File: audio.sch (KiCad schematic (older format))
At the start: 37 parts

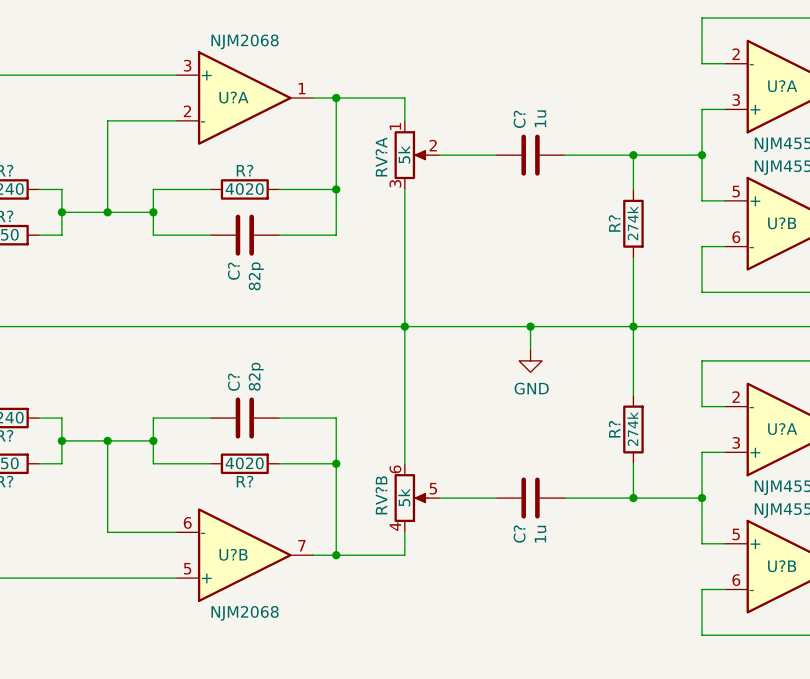
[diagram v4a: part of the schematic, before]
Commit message: replace bourns audio pot for alps (target jade version)
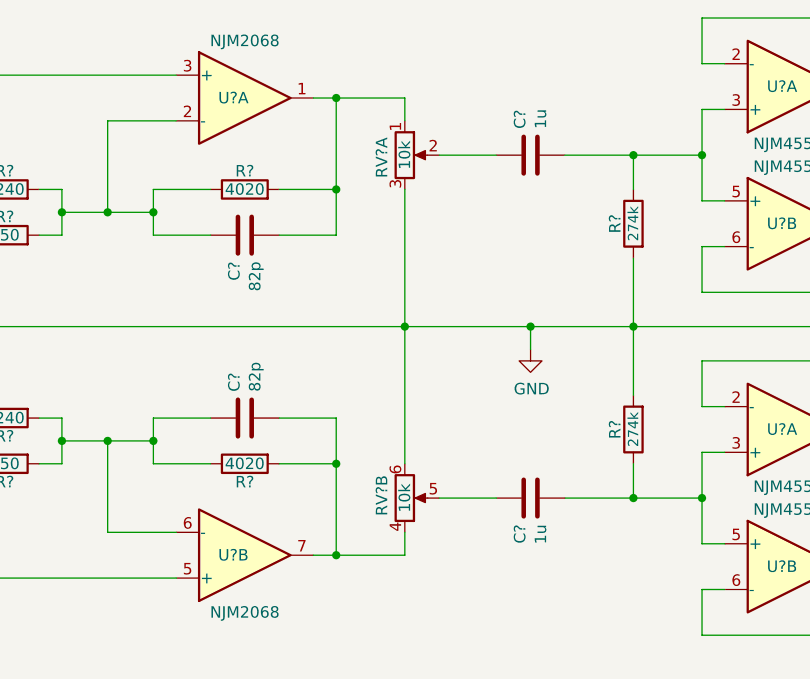
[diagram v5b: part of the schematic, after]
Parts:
- RV?: value 5k -> 10k; footprint bourns:PTD902-1015K-A502 -> Potentiometer_THT:Potentiometer_Alps_RK097_Dual_Horizontal; Description Potentiometer 2 Gang Audio Taper 5kOhms -> Potentiometer 15mm 10k 2-Gang Audio Taper; Manufacturer Bourns -> ALPS; Manufacturer Part Number PTD902-1015K-A502 -> RK09712200MC; Supplier Part Number 652-PTD9021015KA502 -> 688-RK09712200MC
- RV?: value 5k -> 10k; footprint (none) -> Potentiometer_THT:Potentiometer_Alps_RK097_Dual_Horizontal; Description KNOB KNURLED 0.236\" METAL -> (none); Manufacturer SparkFun Electronics -> (none); Manufacturer Part Number COM-10002 -> (none); Supplier Digi-Key -> (none); Supplier Part Number 1568-1601-ND -> (none)
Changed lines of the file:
@@
 P 6300 2650
 F 0 "RV?" V 6200 2550 50  0000 L CNN
-F 1 "5k" V 6300 2650 50  0000 C CNN
-F 2 "bourns:PTD902-1015K-A502" H 6300 2650 50  0001 C CNN
-F 3 "https://www.bourns.com/docs/product-datasheets/PTD90.pdf" H 6300 2650 50  0001 C CNN
-F 4 "Potentiometer 2 Gang Audio Taper 5kOhms" H 0   -600 50  0001 C CNN "Description"
-F 5 "Bourns" H 0   -600 50  0001 C CNN "Manufacturer"
-F 6 "PTD902-1015K-A502" H 0   -600 50  0001 C CNN "Manufacturer Part Number"
+F 1 "10k" V 6300 2650 50  0000 C CNN
+F 2 "Potentiometer_THT:Potentiometer_Alps_RK097_Dual_Horizontal" H 6300 2650 50  0001 C CNN
+F 3 "https://www.mouser.com/datasheet/2/15/RK097-1370742.pdf" H 6300 2650 50  0001 C CNN
+F 4 "Potentiometer 15mm 10k 2-Gang Audio Taper" H 0   -600 50  0001 C CNN "Description"
+F 5 "ALPS" H 0   -600 50  0001 C CNN "Manufacturer"
+F 6 "RK09712200MC" H 0   -600 50  0001 C CNN "Manufacturer Part Number"
 F 7 "Mouser" H 0   -600 50  0001 C CNN "Supplier"
-F 8 "652-PTD9021015KA502" H 0   -600 50  0001 C CNN "Supplier Part Number"
+F 8 "688-RK09712200MC" H 0   -600 50  0001 C CNN "Supplier Part Number"
 	1    6300 2650
 	1    0    0    -1
@@
 P 6300 4150
 F 0 "RV?" V 6200 4050 50  0000 L CNN
-F 1 "5k" V 6300 4150 50  0000 C CNN
-F 2 "" H 6300 4150 50  0001 C CNN
-F 3 "https://www.digikey.com/product-detail/en/sparkfun-electronics/COM-10002/1568-1601-ND/7229871" H 6300 4150 50  0001 C CNN
-F 4 "KNOB KNURLED 0.236\" METAL" H 0   -600 50  0001 C CNN "Description"
-F 5 "SparkFun Electronics" H 0   -600 50  0001 C CNN "Manufacturer"
-F 6 "COM-10002" H 0   -600 50  0001 C CNN "Manufacturer Part Number"
-F 7 "Digi-Key" H 0   -600 50  0001 C CNN "Supplier"
-F 8 "1568-1601-ND" H 0   -600 50  0001 C CNN "Supplier Part Number"
+F 1 "10k" V 6300 4150 50  0000 C CNN
+F 2 "Potentiometer_THT:Potentiometer_Alps_RK097_Dual_Horizontal" H 6300 4150 50  0001 C CNN
+F 3 "https://www.mouser.com/datasheet/2/15/RK097-1370742.pdf" H 6300 4150 50  0001 C CNN
 	2    6300 4150
 	1    0    0    1
